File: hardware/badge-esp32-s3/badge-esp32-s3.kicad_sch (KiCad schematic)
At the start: 4 parts, among them U1 ESP32-S3-MINI-1-N8

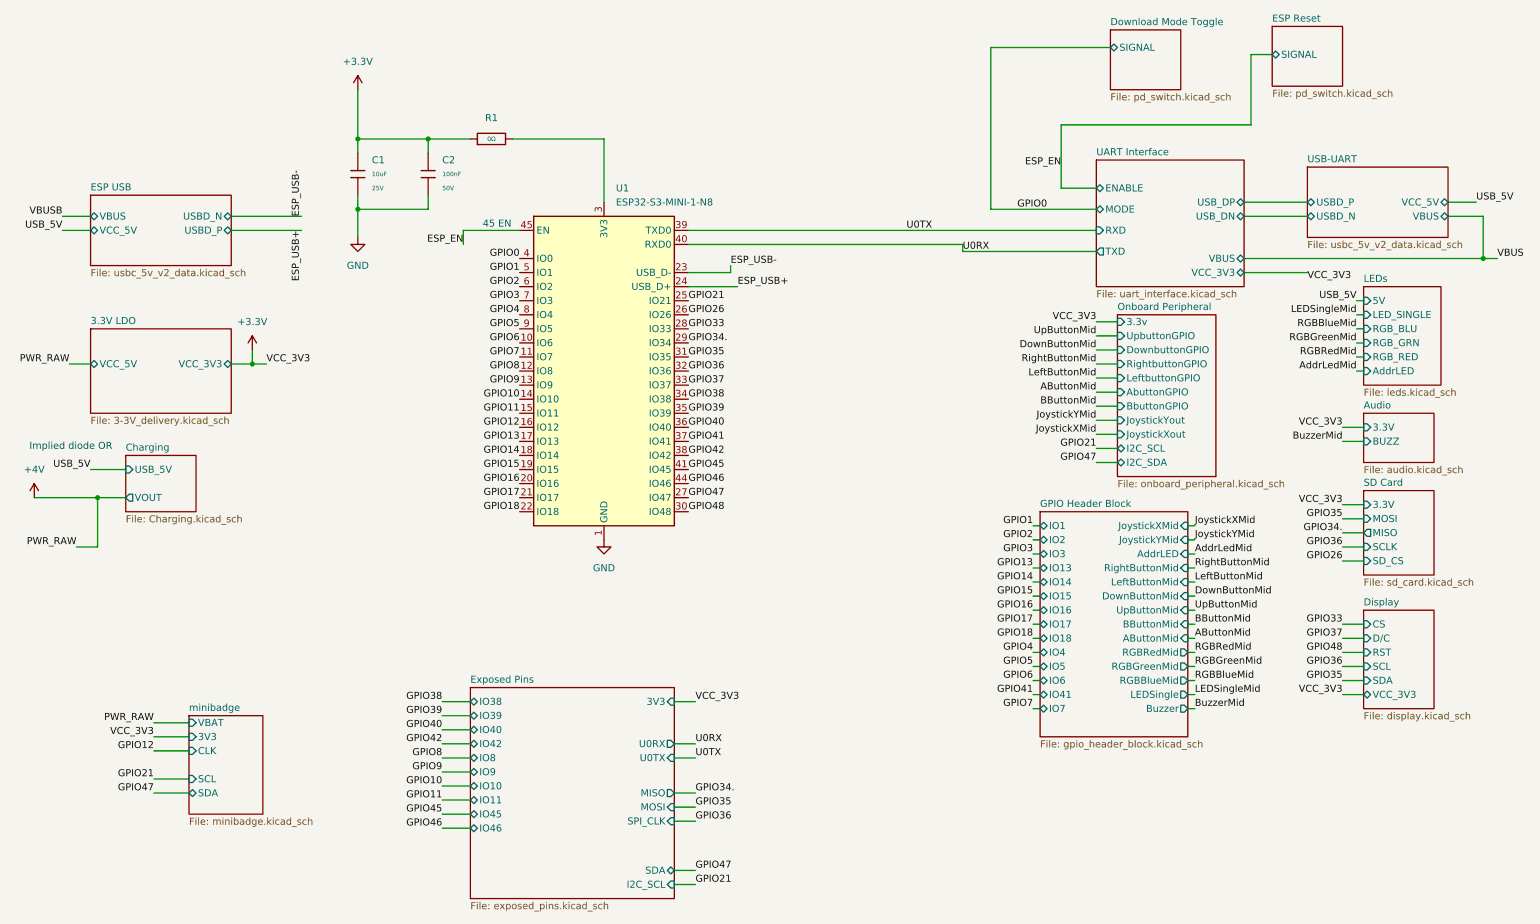
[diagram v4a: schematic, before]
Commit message: Updated pins
Updated pins and headers to avoid using internal flash SPI pins on schematic.
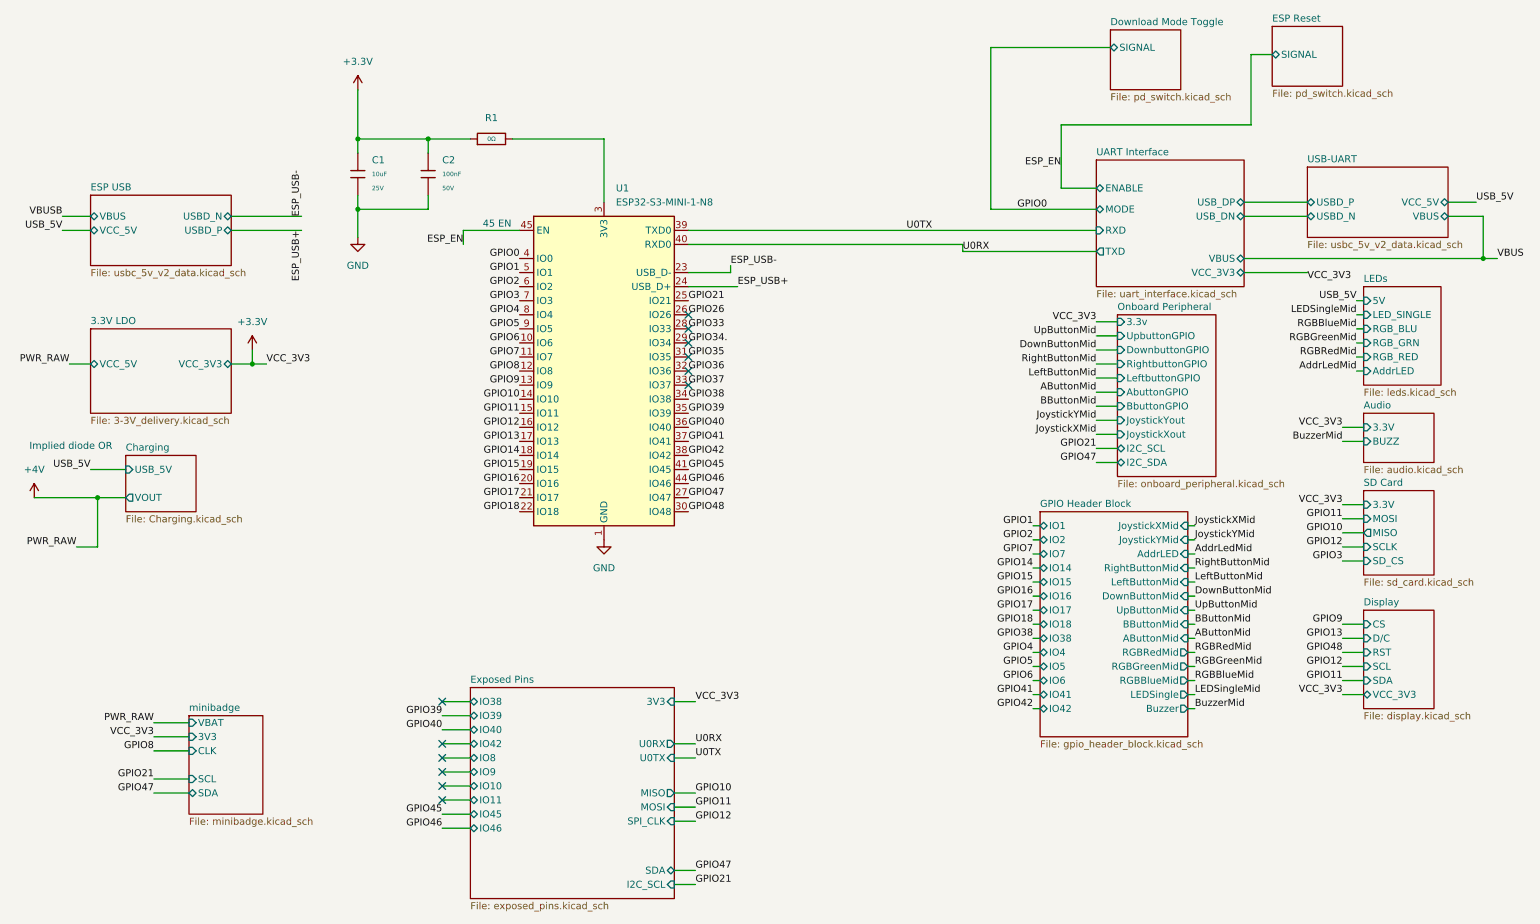
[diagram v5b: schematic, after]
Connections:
- no-connect marks 0 -> 12
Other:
- sheet GPIO Header Block ports: added IO38, IO42; removed IO13, IO3
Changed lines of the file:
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@@
 		(color 0 0 0 0)
 	)
+	(no_connect
+		(at 133.35 67.31)
+	)
+	(no_connect
+		(at 88.9 154.94)
+	)
+	(no_connect
+		(at 88.9 147.32)
+	)
+	(no_connect
+		(at 88.9 137.16)
+	)
+	(no_connect
+		(at 133.35 80.01)
+	)
+	(no_connect
+		(at 133.35 77.47)
+	)
+	(no_connect
+		(at 133.35 74.93)
+	)
+	(no_connect
+		(at 88.9 152.4)
+	)
+	(no_connect
+		(at 133.35 69.85)
+	)
+	(no_connect
+		(at 133.35 72.39)
+	)
+	(no_connect
+		(at 88.9 144.78)
+	)
+	(no_connect
+		(at 88.9 149.86)
+	)
 	(wire
 		(pts
@@
 		)
 	)
-	(label "GPIO18"
+	(label "GPIO38"
 		(at 195.58 125.73 180)
 		(effects
@@
 		)
 	)
-	(label "GPIO26"
+	(label "GPIO3"
 		(at 251.46 111.76 180)
 		(effects
@@
 		)
 	)
-	(label "GPIO13"
+	(label "GPIO14"
 		(at 195.58 113.03 180)
 		(effects
@@
 		)
 	)
-	(label "GPIO34."
+	(label "GPIO10"
 		(at 251.46 106.68 180)
 		(effects
@@
 		)
 	)
-	(label "GPIO11"
-		(at 88.9 154.94 180)
-		(effects
-			(font
-				(size 1.27 1.27)
-			)
-			(justify right bottom)
-		)
-	)
 	(label "GPIO21"
 		(at 134.62 170.18 0)
@@
 		)
 	)
-	(label "GPIO15"
+	(label "GPIO16"
 		(at 195.58 118.11 180)
 		(effects
@@
 		)
 	)
-	(label "GPIO35"
+	(label "GPIO11"
 		(at 134.62 156.21 0)
 		(effects
@@
 		)
 	)
-	(label "GPIO10"
-		(at 88.9 152.4 180)
-		(effects
-			(font
-				(size 1.27 1.27)
-			)
-			(justify right bottom)
-		)
-	)
 	(label "GPIO48"
 		(at 133.35 102.87 0)
@@
 		)
 	)
-	(label "GPIO38"
-		(at 88.9 137.16 180)
-		(effects
-			(font
-				(size 1.27 1.27)
-			)
-			(justify right bottom)
-		)
-	)
 	(label "GPIO34."
 		(at 133.35 72.39 0)
@@
 		)
 	)
-	(label "GPIO3"
+	(label "GPIO7"
 		(at 195.58 110.49 180)
 		(effects
@@
 		)
 	)
-	(label "GPIO36"
+	(label "GPIO12"
 		(at 134.62 158.75 0)
 		(effects
@@
 		)
 	)
-	(label "GPIO16"
+	(label "GPIO17"
 		(at 195.58 120.65 180)
 		(effects
@@
 		)
 	)
-	(label "GPIO17"
+	(label "GPIO18"
 		(at 195.58 123.19 180)
 		(effects
@@
 		)
 	)
-	(label "GPIO9"
-		(at 88.9 149.86 180)
-		(effects
-			(font
-				(size 1.27 1.27)
-			)
-			(justify right bottom)
-		)
-	)
 	(label "GPIO2"
 		(at 102.87 62.23 180)
@@
 		)
 	)
-	(label "GPIO14"
+	(label "GPIO15"
 		(at 195.58 115.57 180)
 		(effects
@@
 		)
 	)
-	(label "GPIO12"
+	(label "GPIO8"
 		(at 36.83 146.05 180)
 		(effects
@@
 		)
 	)
-	(label "GPIO35"
+	(label "GPIO11"
 		(at 251.46 133.35 180)
 		(effects
@@
 		)
 	)
-	(label "GPIO7"
+	(label "GPIO42"
 		(at 195.58 138.43 180)
 		(effects
@@
 		)
 	)
-	(label "GPIO8"
-		(at 88.9 147.32 180)
-		(effects
-			(font
-				(size 1.27 1.27)
-			)
-			(justify right bottom)
-		)
-	)
 	(label "USB_5V"
 		(at 20.32 52.07 180)
@@
 		)
 	)
-	(label "GPIO34."
+	(label "GPIO10"
 		(at 134.62 153.67 0)
 		(effects
@@
 		)
 	)
-	(label "GPIO37"
+	(label "GPIO13"
 		(at 251.46 125.73 180)
 		(effects
@@
 		)
 	)
-	(label "GPIO33"
+	(label "GPIO9"
 		(at 251.46 123.19 180)
 		(effects
@@
 		)
 	)
-	(label "GPIO35"
+	(label "GPIO11"
 		(at 251.46 104.14 180)
 		(effects
@@
 		)
 	)
-	(label "GPIO36"
+	(label "GPIO12"
 		(at 251.46 130.81 180)
 		(effects
@@
 		)
 	)
-	(label "GPIO42"
-		(at 88.9 144.78 180)
-		(effects
-			(font
-				(size 1.27 1.27)
-			)
-			(justify right bottom)
-		)
-	)
 	(label "PWR_RAW"
 		(at 21.59 76.2 180)
@@
 		)
 	)
-	(label "GPIO36"
+	(label "GPIO12"
 		(at 251.46 109.22 180)
 		(effects
@@
 			)
 		)
-		(pin "IO13" bidirectional
+		(pin "IO14" bidirectional
 			(at 196.85 113.03 180)
 			(effects
@@
 			)
 		)
-		(pin "IO14" bidirectional
+		(pin "IO15" bidirectional
 			(at 196.85 115.57 180)
 			(effects
@@
 			)
 		)
-		(pin "IO15" bidirectional
+		(pin "IO16" bidirectional
 			(at 196.85 118.11 180)
 			(effects
@@
 			)
 		)
-		(pin "IO16" bidirectional
+		(pin "IO17" bidirectional
 			(at 196.85 120.65 180)
 			(effects
@@
 			)
 		)
-		(pin "IO17" bidirectional
+		(pin "IO18" bidirectional
 			(at 196.85 123.19 180)
 			(effects
@@
 			)
 		)
-		(pin "IO18" bidirectional
+		(pin "IO38" bidirectional
 			(at 196.85 125.73 180)
 			(effects
@@
 			)
 		)
-		(pin "IO7" bidirectional
+		(pin "IO42" bidirectional
 			(at 196.85 138.43 180)
 			(effects
@@
 			)
 		)
-		(pin "IO3" bidirectional
+		(pin "IO7" bidirectional
 			(at 196.85 110.49 180)
 			(effects

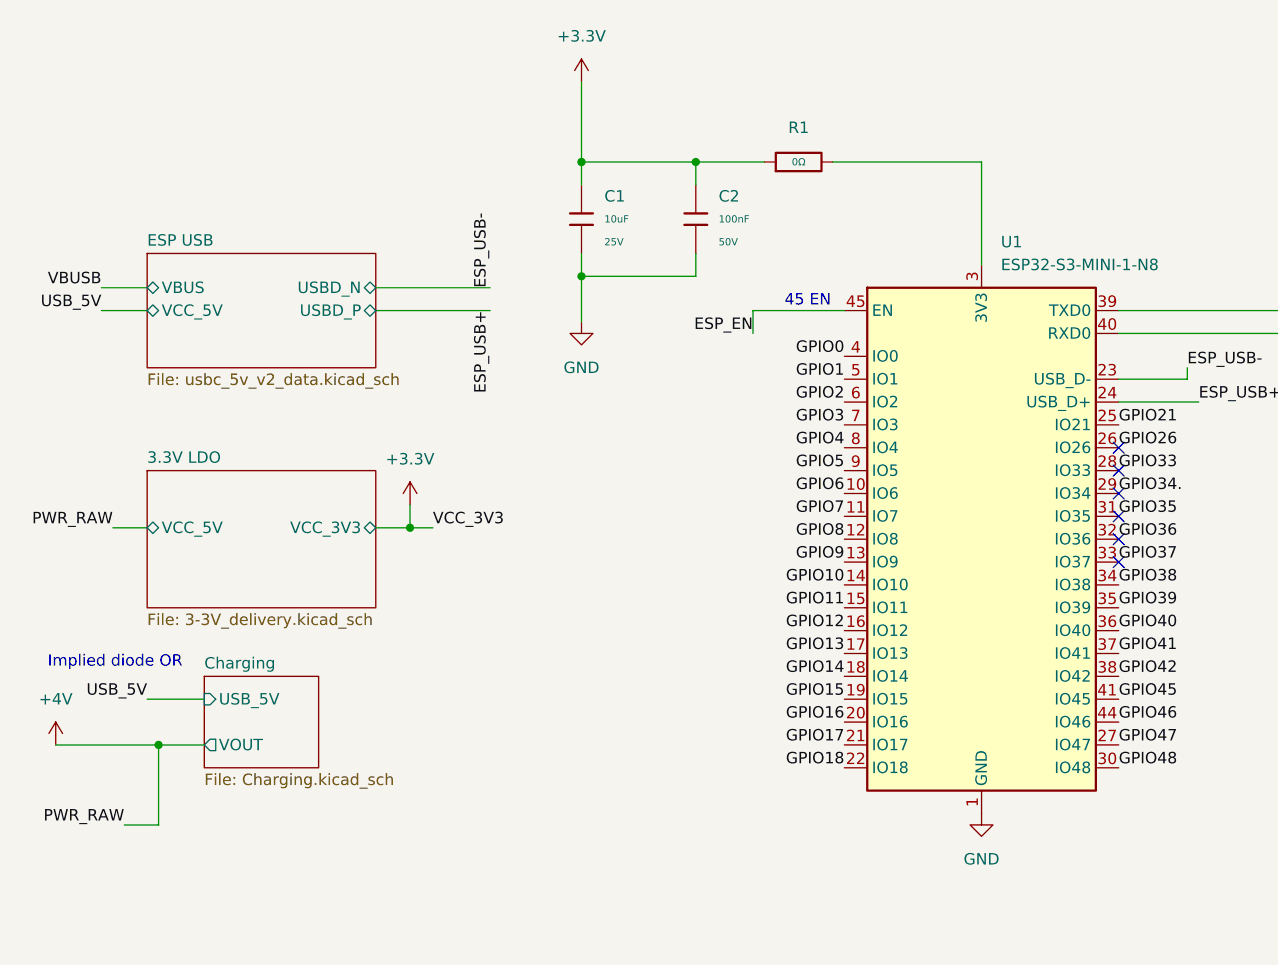
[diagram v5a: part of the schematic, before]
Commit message: Fixed the errors in the schematic, and redid some label
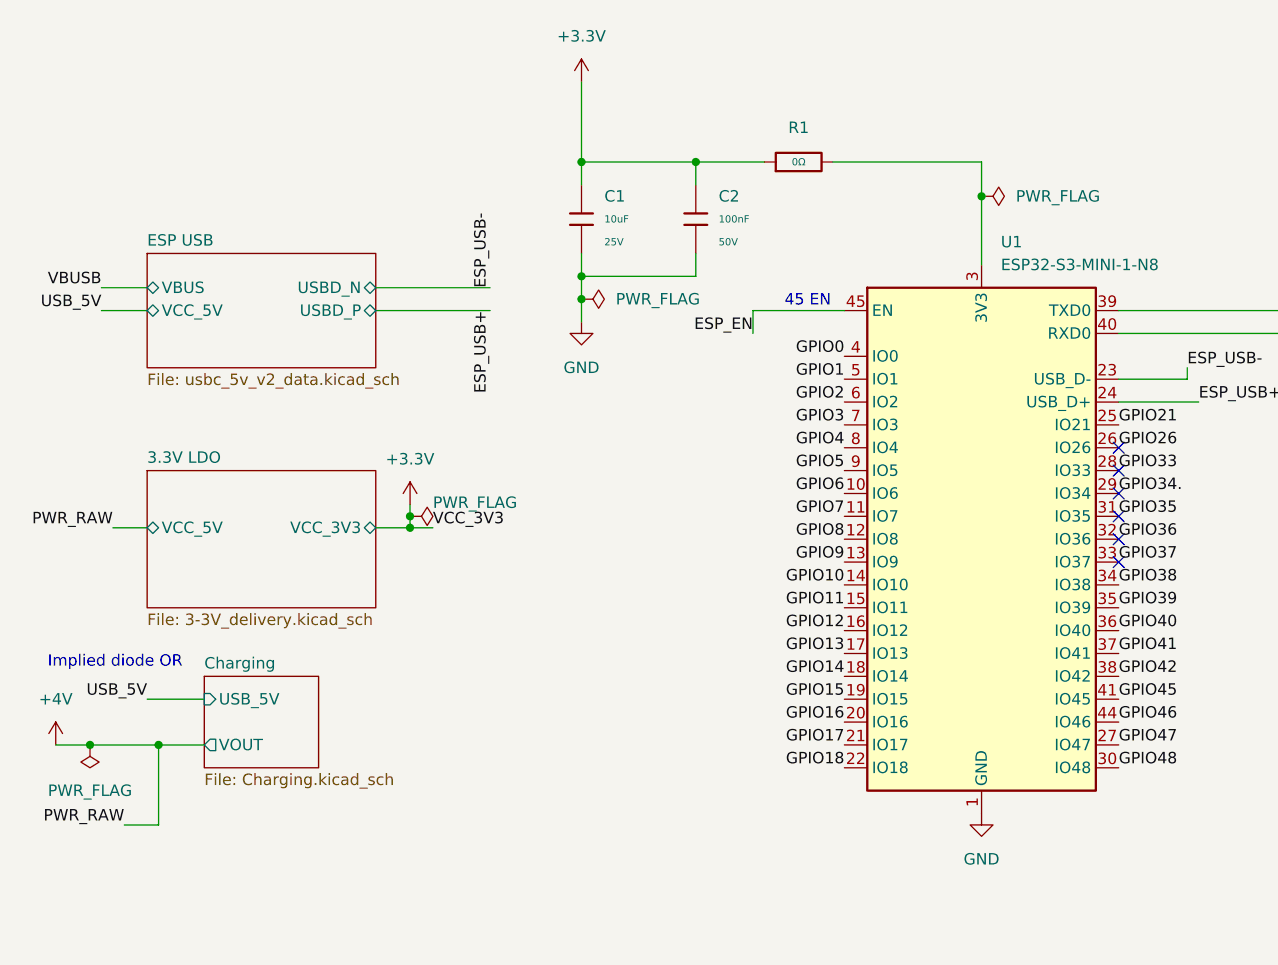
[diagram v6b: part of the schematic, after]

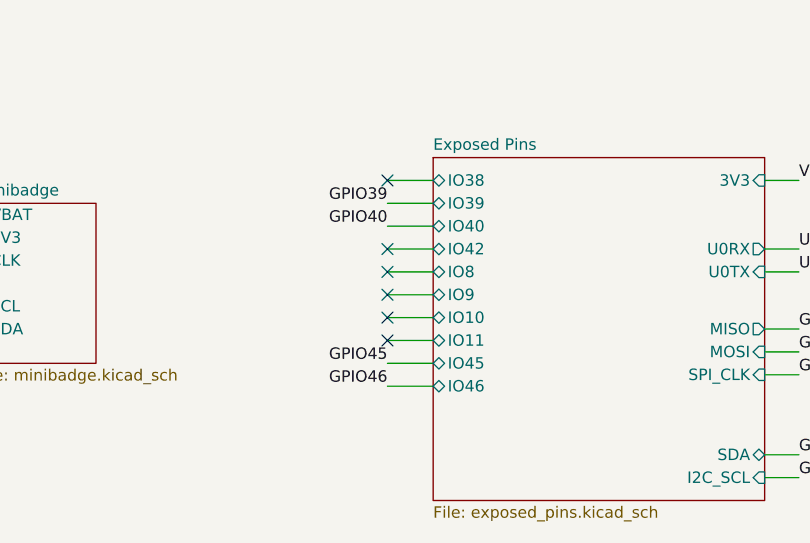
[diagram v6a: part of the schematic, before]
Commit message: Updated the exposed gpio block.
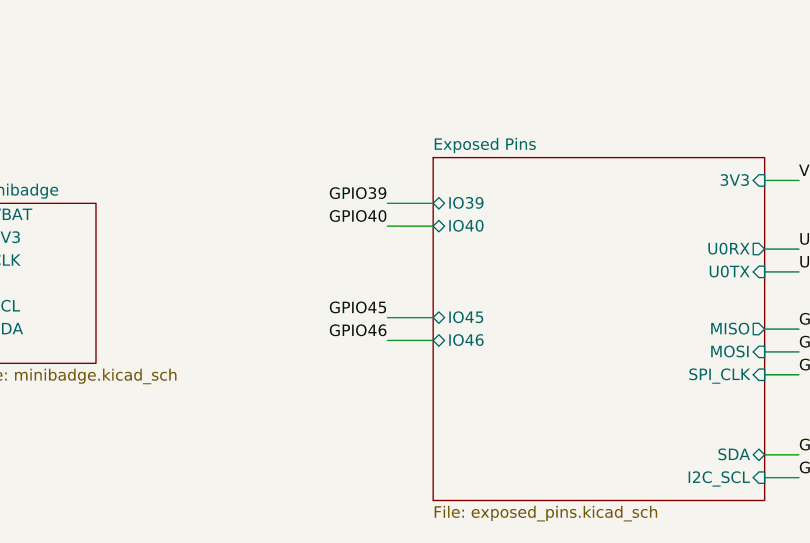
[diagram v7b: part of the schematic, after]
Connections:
- no-connect marks 12 -> 6
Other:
- sheet Exposed Pins ports: added none; removed IO10, IO11, IO38, IO42, IO8, IO9
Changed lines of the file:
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@@
 	)
 	(no_connect
-		(at 88.9 154.94)
-	)
-	(no_connect
-		(at 88.9 147.32)
-	)
-	(no_connect
-		(at 88.9 137.16)
-	)
-	(no_connect
 		(at 133.35 80.01)
 	)
@@
 	)
 	(no_connect
-		(at 88.9 152.4)
-	)
-	(no_connect
 		(at 133.35 69.85)
 	)
@@
 		(at 133.35 72.39)
 	)
-	(no_connect
-		(at 88.9 144.78)
-	)
-	(no_connect
-		(at 88.9 149.86)
-	)
 	(wire
 		(pts
@@
 	(wire
 		(pts
-			(xy 88.9 144.78) (xy 93.98 144.78)
-		)
-		(stroke
-			(width 0)
-			(type default)
-		)
-	)
-	(wire
-		(pts
 			(xy 251.46 130.81) (xy 255.27 130.81)
 		)
@@
 	(wire
 		(pts
-			(xy 88.9 149.86) (xy 93.98 149.86)
-		)
-		(stroke
-			(width 0)
-			(type default)
-		)
-	)
-	(wire
-		(pts
 			(xy 251.46 106.68) (xy 255.27 106.68)
 		)
@@
 	(wire
 		(pts
-			(xy 88.9 137.16) (xy 93.98 137.16)
-		)
-		(stroke
-			(width 0)
-			(type default)
-		)
-	)
-	(wire
-		(pts
 			(xy 207.01 91.44) (xy 210.82 91.44)
 		)
@@
 	(wire
 		(pts
-			(xy 88.9 154.94) (xy 93.98 154.94)
-		)
-		(stroke
-			(width 0)
-			(type default)
-		)
-	)
-	(wire
-		(pts
 			(xy 50.8 52.07) (xy 63.5 52.07)
 		)
@@
 	(wire
 		(pts
-			(xy 88.9 152.4) (xy 93.98 152.4)
-		)
-		(stroke
-			(width 0)
-			(type default)
-		)
-	)
-	(wire
-		(pts
 			(xy 86.36 48.26) (xy 73.66 48.26)
 		)
@@
 	(wire
 		(pts
-			(xy 88.9 147.32) (xy 93.98 147.32)
-		)
-		(stroke
-			(width 0)
-			(type default)
-		)
-	)
-	(wire
-		(pts
 			(xy 73.66 35.56) (xy 73.66 38.1)
 		)
@@
 	(wire
 		(pts
-			(xy 88.9 157.48) (xy 93.98 157.48)
+			(xy 88.9 152.4) (xy 93.98 152.4)
 		)
 		(stroke
@@
 	(wire
 		(pts
-			(xy 88.9 160.02) (xy 93.98 160.02)
+			(xy 88.9 154.94) (xy 93.98 154.94)
 		)
 		(stroke
@@
 	)
 	(label "GPIO45"
-		(at 88.9 157.48 180)
+		(at 88.9 152.4 180)
 		(effects
 			(font
@@
 	)
 	(label "GPIO46"
-		(at 88.9 160.02 180)
+		(at 88.9 154.94 180)
 		(effects
 			(font
@@
 			)
 		)
-		(pin "IO38" bidirectional
-			(at 93.98 137.16 180)
-			(effects
-				(font
-					(size 1.27 1.27)
-				)
-				(justify left)
-			)
-		)
 		(pin "IO39" bidirectional
 			(at 93.98 139.7 180)
@@
 			)
 		)
-		(pin "IO42" bidirectional
-			(at 93.98 144.78 180)
-			(effects
-				(font
-					(size 1.27 1.27)
-				)
-				(justify left)
-			)
-		)
-		(pin "IO8" bidirectional
-			(at 93.98 147.32 180)
-			(effects
-				(font
-					(size 1.27 1.27)
-				)
-				(justify left)
-			)
-		)
-		(pin "IO9" bidirectional
-			(at 93.98 149.86 180)
-			(effects
-				(font
-					(size 1.27 1.27)
-				)
-				(justify left)
-			)
-		)
-		(pin "IO10" bidirectional
-			(at 93.98 152.4 180)
-			(effects
-				(font
-					(size 1.27 1.27)
-				)
-				(justify left)
-			)
-		)
-		(pin "IO11" bidirectional
-			(at 93.98 154.94 180)
-			(effects
-				(font
-					(size 1.27 1.27)
-				)
-				(justify left)
-			)
-		)
 		(pin "MISO" output
 			(at 130.81 153.67 0)
@@
 		)
 		(pin "IO45" bidirectional
-			(at 93.98 157.48 180)
+			(at 93.98 152.4 180)
 			(effects
 				(font
@@
 		)
 		(pin "IO46" bidirectional
-			(at 93.98 160.02 180)
+			(at 93.98 154.94 180)
 			(effects
 				(font

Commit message: Made 5V pins that connect to the +4V line. That is the name of the net coming off of the power switch.
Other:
- sheet Exposed Pins ports: added 5V; removed none
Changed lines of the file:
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@@
 	(wire
 		(pts
+			(xy 130.81 139.7) (xy 134.62 139.7)
+		)
+		(stroke
+			(width 0)
+			(type default)
+		)
+	)
+	(wire
+		(pts
 			(xy 195.58 138.43) (xy 196.85 138.43)
 		)
@@
 		)
 	)
+	(label "+4V"
+		(at 134.62 139.7 0)
+		(effects
+			(font
+				(size 1.27 1.27)
+			)
+			(justify left bottom)
+		)
+	)
 	(label "VCC_3V3"
 		(at 207.01 68.58 180)
@@
 			)
 		)
+		(pin "5V" input
+			(at 130.81 139.7 0)
+			(effects
+				(font
+					(size 1.27 1.27)
+				)
+				(justify right)
+			)
+		)
